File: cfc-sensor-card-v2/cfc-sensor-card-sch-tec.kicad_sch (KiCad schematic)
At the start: 19 parts, among them IC1 AD5593RBCPZ-RL7, U12 DRV8212DSGR, U14 MP2410A

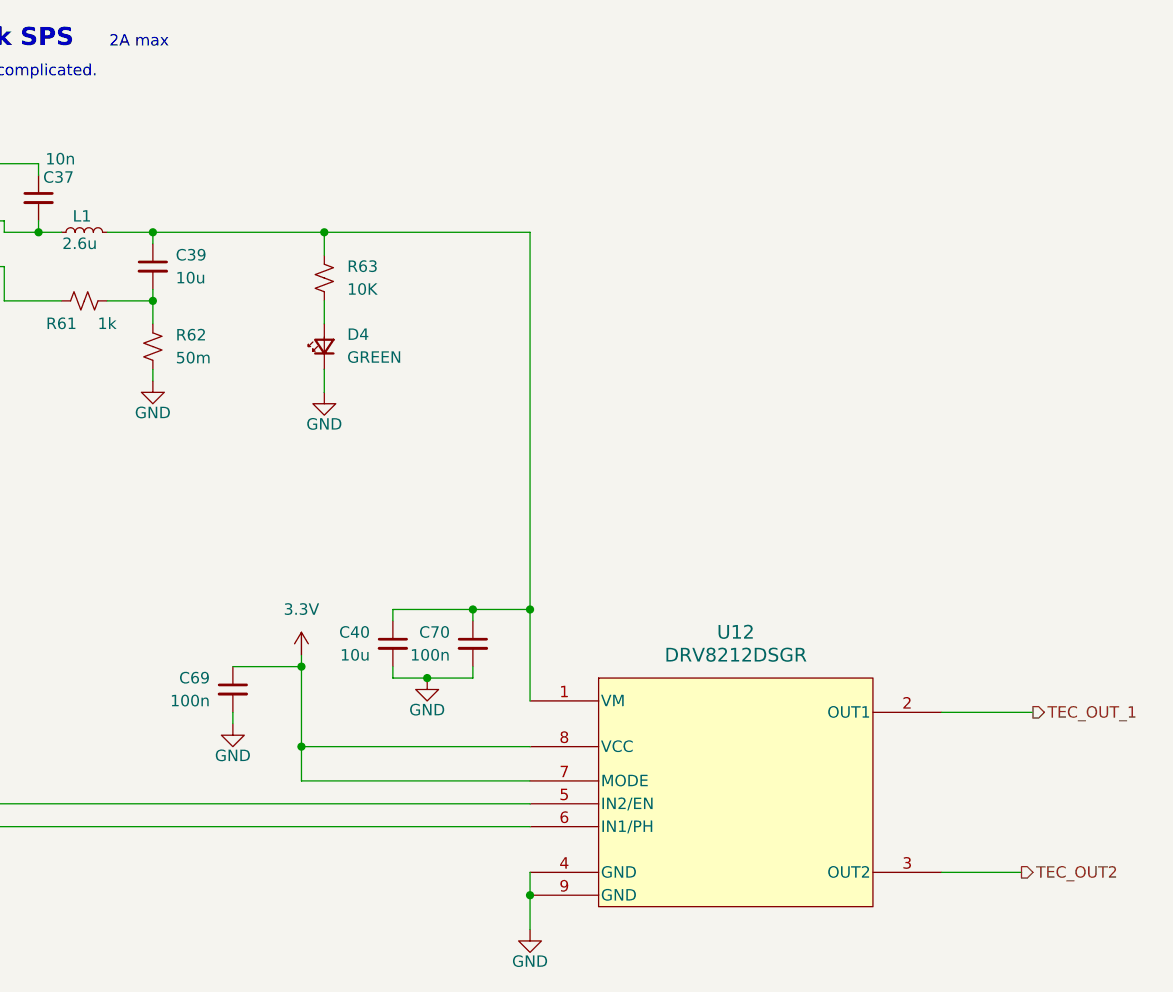
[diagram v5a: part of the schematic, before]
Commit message: update
Changed a couple of test points on OPD to through hole test points. Added tables to DRV8212 on sensor schematic+ other visual improvements to processor schematic.
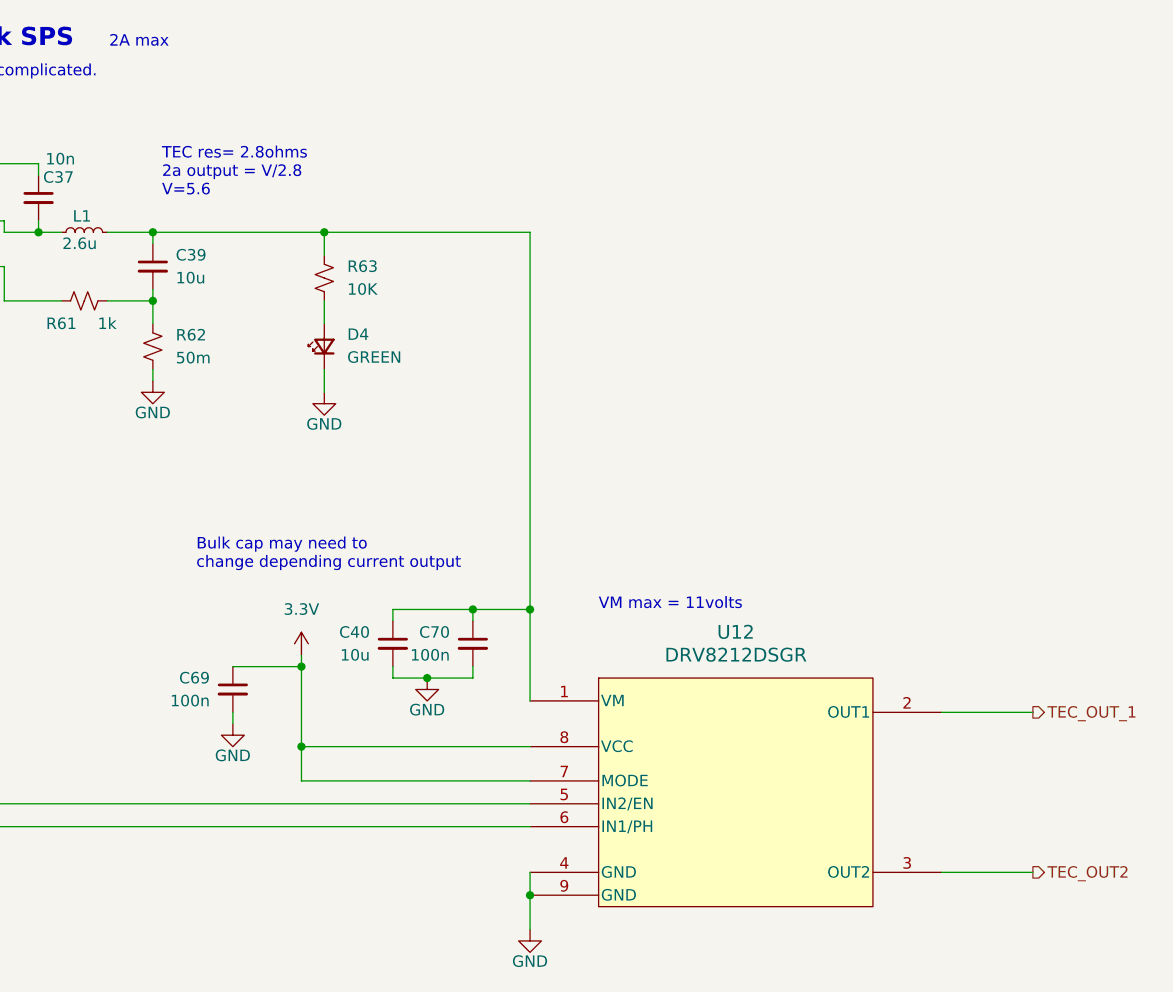
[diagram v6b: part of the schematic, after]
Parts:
- U12: DIS (none) -> DigiKey; DPN (none) -> 296-DRV8212DSGRTR-ND; MFR (none) -> Texas Instruments; MPN (none) -> DRV8212DSGR
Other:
- note added: "Bulk cap may need to change depending current output"
- note added: "TEC res= 2.8ohms 2a output = V/2.8 V=5.6"
- note added: "VM max = 11volts"
